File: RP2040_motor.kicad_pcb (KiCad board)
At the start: 4 copper layers, 85.5 x 54 mm, 180 parts, among them J1 USB_C_Receptacle_USB2.0, J2 Conn_01x05, J3 Conn_01x06, J4 Conn_01x04, J5 Conn_01x04, J6 Conn_01x03, SW1 SW_MEC_5G, U1 EG2131, U10 EG2131, U11 RP2040, U12 EG2131, U13 ADC081S021CISD/NOPB, U2 EG2131, U3 LM358, U4 EG2131, U5 EG2131, U6 NCP1117-3.3_SOT223, U7 XL7045, U8 LM358, U9 W25Q128JVS, Y1 Crystal_GND24

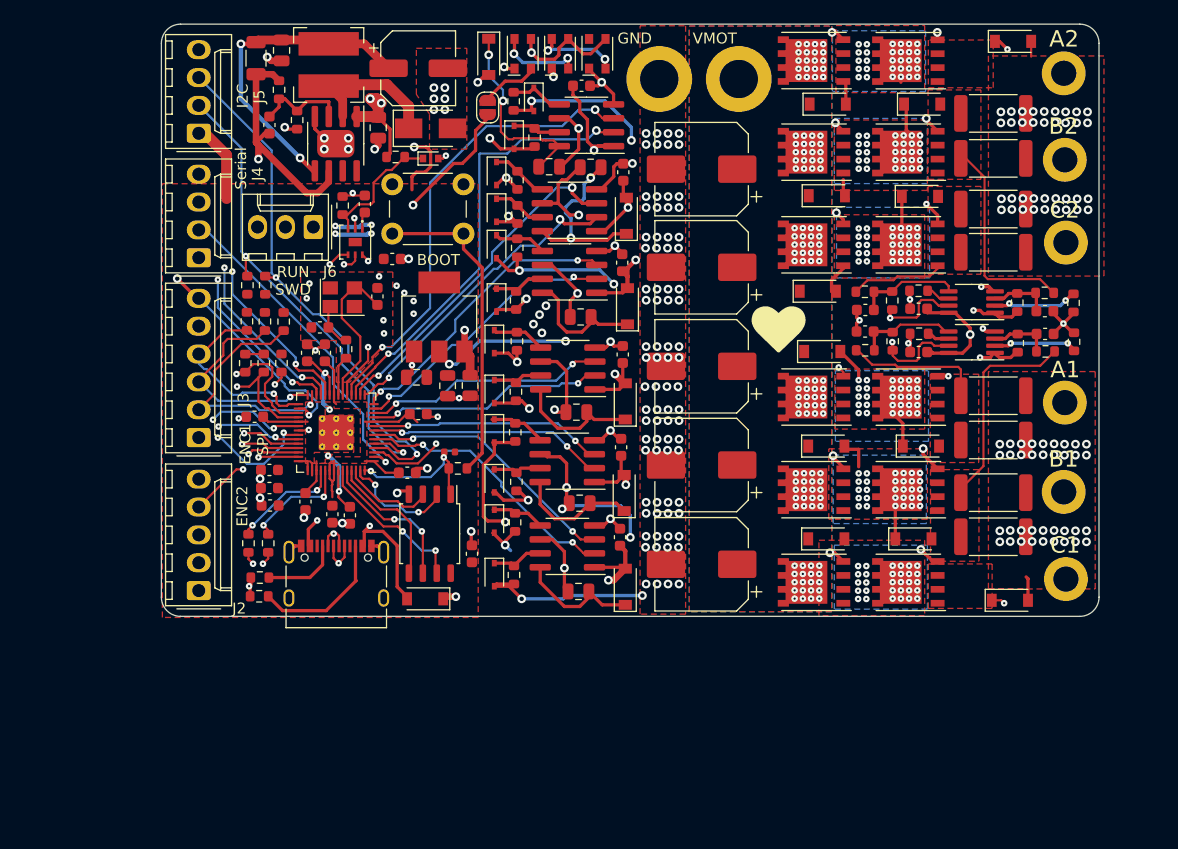
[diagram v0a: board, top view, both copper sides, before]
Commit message: Updated PCB design based on feedback. Added thermistors, mounting holes. This design has better current carrying capacity. gerber folder may not be perfect right now.
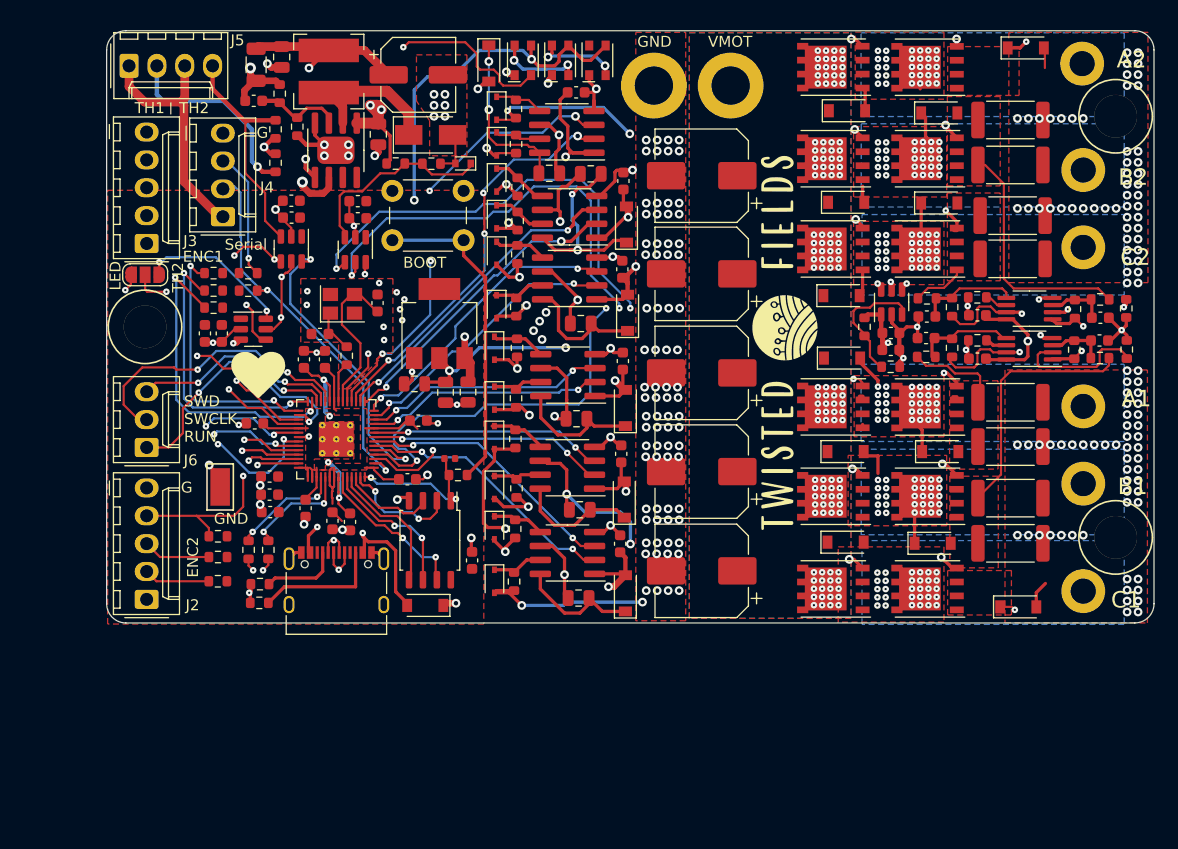
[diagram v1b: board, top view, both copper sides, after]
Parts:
- removed C13: HIGHCURRENTPAD2, RP2040_minimal:PAD_12GA_WIRE
- added C41: 1u, Capacitor_SMD:C_0603_1608Metric, F.Cu at (79.4, 95.6)
- added C42: 1u, Capacitor_SMD:C_0603_1608Metric, F.Cu at (87.3, 83.5)
- added C43: 1u, Capacitor_SMD:C_0603_1608Metric, F.Cu at (141.9, 97.1)
- added G***: LOGO, taylor_footprints:twisted_2, F.Cu at (131.6, 95.1)
- added G***: LOGO, taylor_footprints:twisted, F.Cu at (131.6, 106.7)
- added G***: LOGO, taylor_footprints:twisted_icon, F.Cu at (132.3, 94.9)
- added H1: MountingHole, RP2040_minimal:MountingHole_3.9mm_Plastite_#6, F.Cu at (162.4, 114.2)
- added H2: MountingHole, RP2040_minimal:MountingHole_3.9mm_Plastite_#6, F.Cu at (162.4, 75.8)
- added H3: MountingHole, RP2040_minimal:MountingHole_3.9mm_Plastite_#6, F.Cu at (74.0, 95.0)
- added M2C1: HIGHCURRENTPAD2, RP2040_minimal:PAD_12GA_WIRE, F.Cu at (159.5, 87.8)
- added R60: 0.1uF, Capacitor_SMD:C_0603_1608Metric, F.Cu at (81.0, 95.6)
- added R61: 10k, Resistor_SMD:R_0603_1608Metric, F.Cu at (85.8, 80.0)
- added R62: 0.1uF, Capacitor_SMD:C_0603_1608Metric, F.Cu at (87.3, 85.0)
- added R63: 10k, Resistor_SMD:R_0603_1608Metric, F.Cu at (85.8, 77.0)
- added R64: 0.1uF, Capacitor_SMD:C_0603_1608Metric, F.Cu at (142.0, 95.6)
- added R65: 10k, Resistor_SMD:R_0603_1608Metric, F.Cu at (141.9, 98.6)
- added TH1: Thermistor 10k, Resistor_SMD:R_0603_1608Metric, F.Cu at (139.6, 95.0)
- added TP2: TestPoint, TestPoint:TestPoint_Keystone_5019_Minature, F.Cu at (80.8, 109.6)
- added U14: ADC081S021CISD/NOPB, Package_TO_SOT_SMD:SOT-23-6, F.Cu at (83.8, 95.2)
- added U15: ADC081S021CISD/NOPB, Package_TO_SOT_SMD:SOT-23-6, F.Cu at (87.3, 87.9)
- added U16: ADC081S021CISD/NOPB, Package_TO_SOT_SMD:SOT-23-6, F.Cu at (142.0, 92.7)
- J3: value Conn_01x06 -> Conn_01x05; footprint Connector_Molex:Molex_KK-254_AE-6410-06A_1x06_P2.54mm_Vertical -> Connector_Molex:Molex_KK-254_AE-6410-05A_1x05_P2.54mm_Vertical
- JP1: value SolderJumper_2_Open -> SolderJumper_3_Open; footprint Jumper:SolderJumper-2_P1.3mm_Open_RoundedPad1.0x1.5mm -> Jumper:SolderJumper-3_P1.3mm_Open_RoundedPad1.0x1.5mm_NumberLabels
- R20, R22, R24, R26, R3, R4, R54, R55, R56, R57: value 22R -> 10.2R
- U13: footprint ADC081S021:ADC081S021CISD&slash_NOPB -> Package_TO_SOT_SMD:SOT-23-6
- U9: value W25Q128JVS -> W25Q16JVSSIQ
- moved JP1 34.8 mm to (74.0, 90.2), turned to 0 degrees
- moved J6 25.2 mm to (74.1, 106.0), turned to 90 degrees
- moved R45 20.0 mm to (80.6, 118.2), turned to 180 degrees
- moved J3 18.3 mm to (74.1, 87.4)
- moved R43 18.2 mm to (80.6, 116.0), turned to 180 degrees
- moved R41 16.8 mm to (80.6, 114.1), turned to 180 degrees
- moved R59 8.95 mm to (100.1, 80.1), turned to 0 degrees
- moved J5 8.85 mm to (72.5, 71.2), turned to 0 degrees
- moved R44 6.51 mm to (80.2, 93.2), turned to 180 degrees
- moved R46 6.13 mm to (93.3, 83.5), turned to 180 degrees
- moved R13 5.69 mm to (145.2, 92.4)
- moved R14 5.64 mm to (145.2, 94.1)
- moved R8 5.59 mm to (145.2, 96.0)
- moved R7 5.59 mm to (145.2, 97.7)
- moved R29 5.49 mm to (147.5, 93.2)
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- renumbered A1 to M1A1, B1 to M1B1, C12 to M1C1, A2 to M2A1, B2 to M2B1
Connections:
- net ADC_CS renamed ADC_CS1
- D34 pad 2: Net-(D34-Pad2) -> LED
- J5 pad 2: SCLK -> TH1
- J5 pad 3: SDA -> +3V3
- J5 pad 4: GND -> TH2
- JP1 pad 1: SPI0TX -> LED
- JP1 pad 2: Net-(D34-Pad2) -> LED_OR_ADC_CS4
- R49 pad 2: SDA -> TXO
- R50 pad 1: SCLK -> RXI
- U11 pad 30: SPI0TX -> LED_OR_ADC_CS4
- U11 pad 4: SDA -> ADC_CS2
- U11 pad 5: SCLK -> ADC_CS3
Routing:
- net ADC_CLK: track 30.4 -> 111.2 mm, vias 3 -> 8
- net SPI0TX: track 67.3 -> 0.00 mm, vias 3 -> 0
- net ADC_CS2: track 0.00 -> 62.4 mm, vias 0 -> 3
- net LED: track 0.00 -> 61.9 mm, vias 0 -> 2
- net ADC_DATA: track 48.4 -> 106.1 mm, vias 3 -> 7
- net SDA: track 49.1 -> 0.00 mm, vias 2 -> 0
- net SCLK: track 45.0 -> 0.00 mm, vias 2 -> 0
- net TH1: track 0.00 -> 35.8 mm, vias 0 -> 2
- net ADC_CS3: track 0.00 -> 28.4 mm, vias 0 -> 2
- net GND: track 78.6 -> 105.0 mm, vias 202 -> 229
- net LED_OR_ADC_CS4: track 0.00 -> 26.2 mm, vias 0 -> 4
- net TH2: track 0.00 -> 21.1 mm
- net +3V3: track 140.0 -> 160.6 mm, vias 9 -> 6
- net SPI0SCK: track 17.3 -> 36.5 mm, vias 1 -> 2
- net SPI0CS: track 19.6 -> 35.3 mm, vias 1 -> 2
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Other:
- board size 85.5 x 54 mm -> 95.5 x 54 mm
- board text added: "ENC1"
- board text added: "G"
- board text added: "Love everyone."
- board text added: "RUN"
- board text added: "SWCLK"
- board text added: "SWD"
- board text added: "SWD SWCLK RUN"
- board text added: "TH1 TH2"
- board text added: "TH2 | TH1"
- board text added: "|"
- board text removed: "ENC1 SPI"
- board text removed: "I2C"
- board text removed: "RUN SWD"
- board text removed: "SPI/ENC1"

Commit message: Additional updates to clean up power and capacitance on buck circuit.
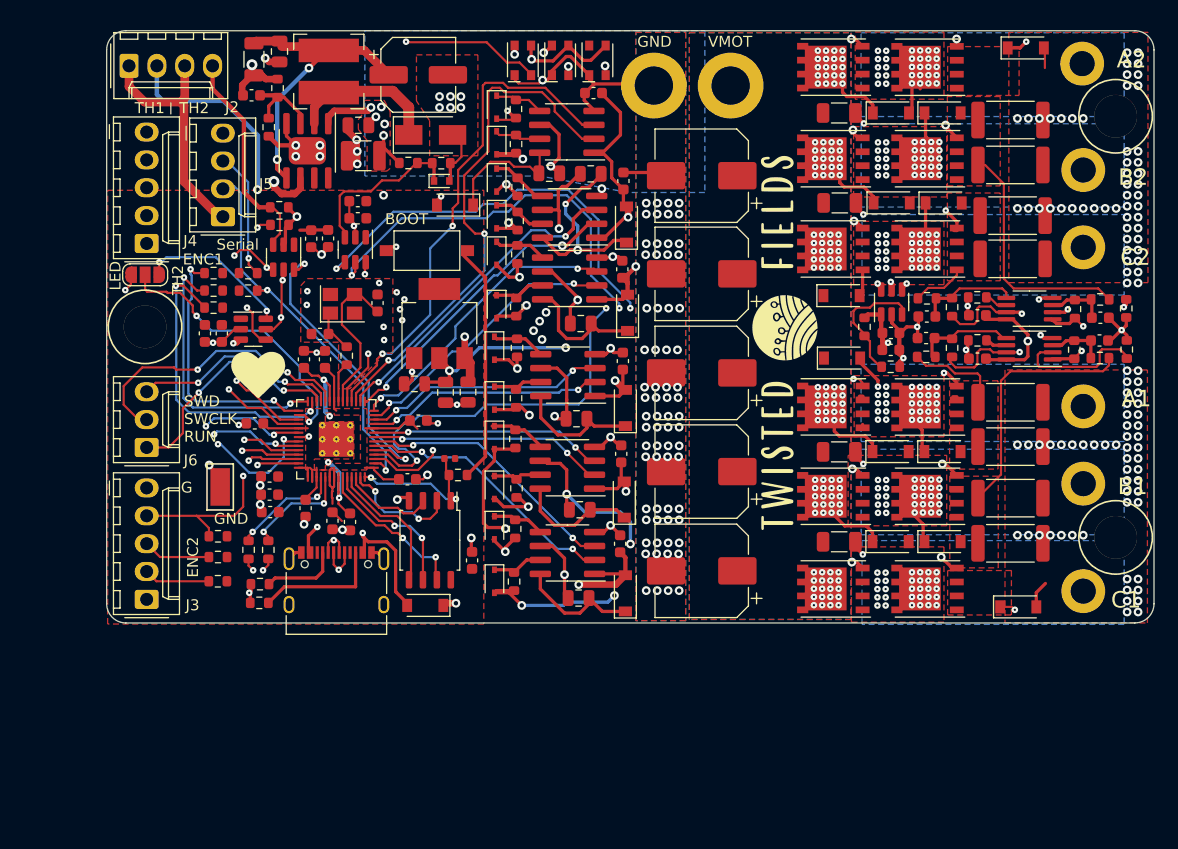
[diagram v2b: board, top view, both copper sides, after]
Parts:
- added C$1: 2.2uF 100V, Capacitor_SMD:C_1206_3216Metric, F.Cu at (137.2, 75.5)
- added C$2: 2.2uF 100V, Capacitor_SMD:C_1206_3216Metric, F.Cu at (137.2, 106.4)
- added C$3: 2.2uF 100V, Capacitor_SMD:C_1206_3216Metric, F.Cu at (137.3, 83.7)
- added C$4: 2.2uF 100V, Capacitor_SMD:C_1206_3216Metric, F.Cu at (137.2, 114.6)
- added C$5: 4.7uF 100V, Capacitor_SMD:C_1210_3225Metric, F.Cu at (93.8, 79.4)
- SW1: footprint Button_Switch_THT:SW_PUSH_6mm_H4.3mm -> parts:SW_TS_1101_C_W
- moved D24 13.3 mm to (102.2, 83.9), turned to 180 degrees
- moved R51 7.12 mm to (86.2, 84.1), turned to 0 degrees
- moved SW1 6.29 mm to (99.7, 88.0)
- moved R46 5.67 mm to (86.2, 85.7), turned to 0 degrees
- moved D19 4.15 mm to (142.0, 83.7)
- moved D7 4.10 mm to (141.9, 114.6)
- moved D17 4.10 mm to (141.9, 106.4)
- moved D29 4.00 mm to (142.0, 75.5)
- moved C22 3.90 mm to (89.1, 87.0), turned to 90 degrees
- moved R47 3.83 mm to (90.6, 86.9), turned to -90 degrees
- moved R49 2.60 mm to (85.2, 76.8)
- moved U11 2.60 mm to (88.8, 79.0)
- moved D36 2.52 mm to (101.0, 81.7), turned to 0 degrees
- moved C$6 1.99 mm to (93.4, 76.6), turned to 180 degrees
- moved C15 1.58 mm to (114.8, 73.7), turned to 0 degrees
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- renumbered C$1 to C$6, C$2 to C$7, C2 to C1, C14 to C10, C15 to C11, C17 to C12, C18 to C13, C21 to C14, C24 to C15, C26 to C16, C28 to C17, C43 to C18, C41 to C19, C3 to C2, C16 to C20, C20 to C21, C42 to C22, C19 to C23, C22 to C24, C27 to C26, C9 to C27, C10 to C28, C23 to C29, C6 to C3, C29 to C30, C30 to C31, C31 to C32, C32 to C33, C33 to C34, C34 to C35, C35 to C36, C36 to C37, C37 to C38, C38 to C39, C11 to C4, C39 to C40, C40 to C41, C1 to C5, C4 to C6, C5 to C7, C7 to C8, C8 to C9, D13 to D12, D14 to D13, D12 to D14, D20 to D19, D21 to D20, D23 to D21, D25 to D22, D26 to D23, D27 to D25, D28 to D26, D29 to D27, D30 to D28, D31 to D29, D32 to D30, D19 to D31, D22 to D32, D34 to D33, D35 to D34, D36 to D35, D33 to D36, J5 to J2, J2 to J3, J3 to J4, J4 to J5, R34 to R1, R29 to R10, R5 to R11, R6 to R12, R28 to R13, R11 to R14, R30 to R15, R12 to R16, R31 to R17, R37 to R18, R20 to R19, R36 to R2, R22 to R20, R38 to R21, R33 to R22, R52 to R23, R26 to R25, R53 to R26, R39 to R27, R58 to R28, R15 to R29, R13 to R3, R19 to R30, R7 to R31, R8 to R32, R9 to R33, R54 to R34, R55 to R35, R10 to R36, R56 to R37, R57 to R38, R64 to R39, R1 to R4, R60 to R40, R23 to R41, R25 to R42, R16 to R43, R17 to R44, R65 to R45, R61 to R46, R62 to R47, R27 to R48, R32 to R49, R2 to R5, R35 to R50, R63 to R51, R21 to R52, R40 to R53, R41 to R54, R42 to R55, R43 to R56, R44 to R57, R45 to R58, R46 to R59, R14 to R6, R47 to R60, R48 to R61, R49 to R62, R50 to R63, R51 to R64, R59 to R65, R3 to R7, R4 to R8, R18 to R9, U14 to U10, U7 to U11, U9 to U12, U6 to U13, U15 to U14, U11 to U15, U13 to U16, U8 to U3, U3 to U6, U10 to U7, U12 to U8, U16 to U9
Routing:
- net GND: track 105.0 -> 131.4 mm, vias 229 -> 226
- net VMOT: track 47.9 -> 29.6 mm, vias 122 -> 125
- net GPIO14: track 36.7 -> 48.5 mm, vias 4 -> 2
- net /power_and_cpu/~{USB_BOOT}: track 29.4 -> 21.5 mm
- net Net-(AH2-Pad2): track 44.3 -> 51.8 mm
- net +12V: track 215.3 -> 209.0 mm, vias 11 -> 10
- net GPIO15: track 40.9 -> 46.1 mm, vias 4 -> 2
- net Net-(C17-Pad2): track 15.9 -> 11.4 mm, vias 2 -> 0
- net ADC_DATA: track 106.1 -> 102.6 mm
- net Net-(D36-Pad1): track 18.4 -> 15.1 mm
- net +3V3: track 160.6 -> 163.8 mm
- net M1B: track 48.3 -> 45.1 mm
- net ADC_CLK: track 111.2 -> 108.4 mm
- net Net-(BL1-Pad2): track 59.9 -> 57.8 mm
- net LED: track 61.9 -> 59.9 mm
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- added copper zone on B.Cu, net GND

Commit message: updated design with dual CPUs
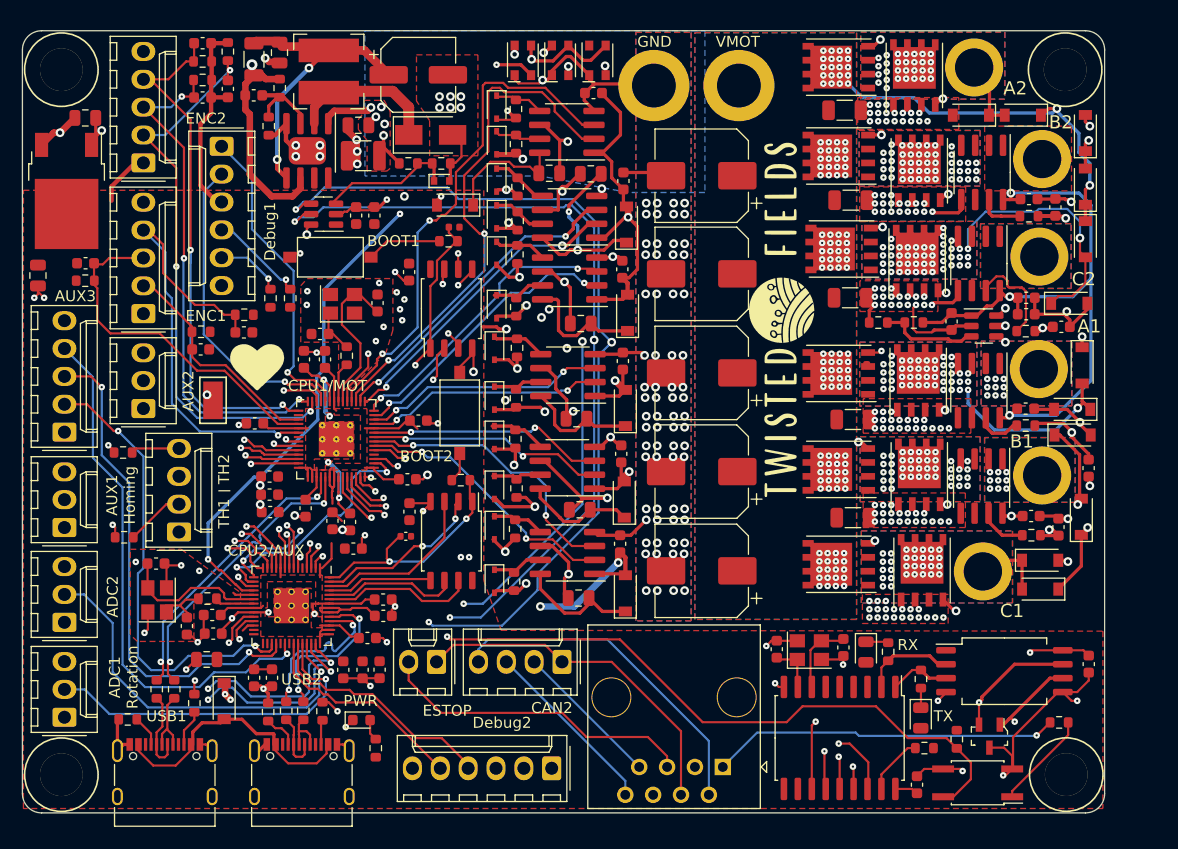
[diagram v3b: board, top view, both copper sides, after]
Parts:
- removed D31: B5819W SL, Diode_SMD:D_SOD-123
- removed JP1: SolderJumper_3_Open, Jumper:SolderJumper-3_P1.3mm_Open_RoundedPad1.0x1.5mm_NumberLabels
- removed R10, R22, R26, R36: 133k, Resistor_SMD:R_0603_1608Metric
- removed R11, R12, R14, R16, R29, R30: 4mΩ, Resistor_SMD:R_2512_6332Metric
- removed R13, R18, R31: 499R, Resistor_SMD:R_0603_1608Metric
- removed R15, R21, R27, R28, R32: 0.1uF, Capacitor_SMD:C_0603_1608Metric
- removed R17, R23, R33, R9: 4.64k, Resistor_SMD:R_0603_1608Metric
- removed U6: LM358, Package_SO:MSOP-8_3x3mm_P0.65mm
- added C$8: 2.2uF 100V, Capacitor_SMD:C_1206_3216Metric, F.Cu at (138.5, 103.5)
- added C42: 20p, Capacitor_SMD:C_0603_1608Metric, F.Cu at (77.8, 122.3)
- added C43: 100n, Capacitor_SMD:C_0603_1608Metric, F.Cu at (98.1, 111.9)
- added C44: 100n, Capacitor_SMD:C_0603_1608Metric, F.Cu at (94.2, 123.4)
- added C45: 100n, Capacitor_SMD:C_0603_1608Metric, F.Cu at (80.2, 123.0)
- added C46: 100n, Capacitor_SMD:C_0603_1608Metric, F.Cu at (95.7, 121.4)
- added C47: 100n, Capacitor_SMD:C_0603_1608Metric, F.Cu at (83.9, 127.0)
- added C48: 100n, Capacitor_SMD:C_0603_1608Metric, F.Cu at (85.5, 127.0)
- added C49: 100n, Capacitor_SMD:C_0603_1608Metric, F.Cu at (92.9, 115.2)
- added C50: 100n, Capacitor_SMD:C_0603_1608Metric, F.Cu at (80.1, 121.3)
- added C51: 100n, Capacitor_SMD:C_0603_1608Metric, F.Cu at (92.0, 126.3)
- added C52: 100n, Capacitor_SMD:C_0603_1608Metric, F.Cu at (93.8, 126.3)
- added C53: 1u, Capacitor_SMD:C_0603_1608Metric, F.Cu at (95.7, 119.9)
- added C54: 1u, Capacitor_SMD:C_0603_1608Metric, F.Cu at (95.3, 126.3)
- added C55: 0.1uF, Capacitor_SMD:C_0603_1608Metric, F.Cu at (160.0, 125.8)
- added C56: 100n, Capacitor_SMD:C_0603_1608Metric, F.Cu at (144.3, 136.8)
- added C57: 10p, Capacitor_SMD:C_0603_1608Metric, F.Cu at (137.6, 124.2)
- added C58: 10p, Capacitor_SMD:C_0603_1608Metric, F.Cu at (131.6, 124.4)
- added C59: 0.1uF, Capacitor_SMD:C_0603_1608Metric, F.Cu at (154.3, 92.3)
- added C60: 47p, Capacitor_SMD:C_0603_1608Metric, F.Cu at (83.0, 95.5)
- added C61: 47p, Capacitor_SMD:C_0603_1608Metric, F.Cu at (68.5, 89.2)
- added C62: 47p, Capacitor_SMD:C_0603_1608Metric, F.Cu at (79.0, 97.1)
- added C63: 47p, Capacitor_SMD:C_0603_1608Metric, F.Cu at (79.2, 74.1)
- added C64: 47p, Capacitor_SMD:C_0603_1608Metric, F.Cu at (81.5, 73.3)
- added C65: 0.1uF, Capacitor_SMD:C_0603_1608Metric, F.Cu at (157.5, 95.0)
- added C66: 0.1uF, Capacitor_SMD:C_0603_1608Metric, F.Cu at (154.6, 83.3)
- added C67: 0.1uF, Capacitor_SMD:C_0603_1608Metric, F.Cu at (154.8, 112.2)
- added C68: 0.1uF, Capacitor_SMD:C_0603_1608Metric, F.Cu at (154.2, 102.5)
- added C69: 0.1uF, Capacitor_SMD:C_0603_1608Metric, F.Cu at (157.2, 113.3)
- added C70: 0.1uF, Capacitor_SMD:C_0603_1608Metric, F.Cu at (157.0, 84.1)
- added C71: 0.1uF, Capacitor_SMD:C_0603_1608Metric, F.Cu at (160.0, 107.9)
- added D37: B5819W SL, Diode_SMD:D_SOD-123, F.Cu at (81.2, 129.1)
- added D38: LED_GREEN, LED_SMD:LED_0805_2012Metric, F.Cu at (144.7, 130.7)
- added D39: LED_ORANGE_RED, LED_SMD:LED_0805_2012Metric, F.Cu at (139.7, 124.7)
- added D40: CDSOT23-SM712, digikey-footprints:SOT-23-3, F.Cu at (150.9, 132.3)
- added D41: LED_RED, LED_SMD:LED_0603_1608Metric, F.Cu at (93.7, 130.9)
- added H4: MountingHole, RP2040_minimal:MountingHole_3.9mm_Plastite_#6, F.Cu at (66.3, 71.5)
- added J10: Conn_01x03, Connector_Molex:Molex_KK-254_AE-6410-03A_1x03_P2.54mm_Vertical, F.Cu at (66.6, 113.3)
- added J11: Conn_01x04, Connector_Molex:Molex_KK-254_AE-6410-04A_1x04_P2.54mm_Vertical, F.Cu at (112.0, 125.5)
- added J12: Conn_01x06, Connector_Molex:Molex_KK-254_AE-6410-06A_1x06_P2.54mm_Vertical, F.Cu at (111.0, 135.3)
- added J13: Conn_01x03, Connector_Molex:Molex_KK-254_AE-6410-03A_1x03_P2.54mm_Vertical, F.Cu at (66.6, 121.9)
- added J14: Conn_01x03, Connector_Molex:Molex_KK-254_AE-6410-03A_1x03_P2.54mm_Vertical, F.Cu at (73.8, 102.5)
- added J15: Conn_01x05, Connector_Molex:Molex_KK-254_AE-6410-05A_1x05_P2.54mm_Vertical, F.Cu at (66.6, 104.6)
- added J7: Conn_01x02, Connector_Molex:Molex_KK-254_AE-6410-02A_1x02_P2.54mm_Vertical, F.Cu at (100.5, 125.5)
- added J8: RJ45, Connector_RJ:RJ45_OST_PJ012-8P8CX_Vertical, F.Cu at (126.6, 135.1)
- added J9: Conn_01x03, Connector_Molex:Molex_KK-254_AE-6410-03A_1x03_P2.54mm_Vertical, F.Cu at (66.6, 130.6)
- added R46: 5.1k, Resistor_SMD:R_0603_1608Metric, F.Cu at (90.1, 130.0)
- added R51: DNS, Capacitor_SMD:C_0402_1005Metric, F.Cu at (97.7, 114.1)
- added R66: 1.1k, Resistor_SMD:R_0603_1608Metric, F.Cu at (102.7, 109.0)
- added R67: 1k, Resistor_SMD:R_0603_1608Metric, F.Cu at (144.7, 127.1)
- added R68: 1k, Resistor_SMD:R_0603_1608Metric, F.Cu at (141.7, 124.6)
- added R70: 27, Resistor_SMD:R_0603_1608Metric, F.Cu at (88.4, 130.0)
- added R71: 27, Resistor_SMD:R_0603_1608Metric, F.Cu at (86.8, 130.0)
- added R72: 10k, Resistor_SMD:R_0603_1608Metric, F.Cu at (145.0, 133.4)
- added R75: 100R, Resistor_SMD:R_0603_1608Metric, F.Cu at (157.3, 131.1)
- added R76: 5.1k, Resistor_SMD:R_0603_1608Metric, F.Cu at (148.0, 132.6)
- added R77: 68R, Resistor_SMD:R_0603_1608Metric, F.Cu at (95.0, 133.4)
- added SW2: SW_MEC_5G, parts:SW_TS_1101_C_W, F.Cu at (102.6, 102.8)
- added U17: isolator, Package_SO:SOIC-8_7.5x5.85mm_P1.27mm, F.Cu at (152.3, 126.4)
- added U18: MCP2515-xSO, Package_SO:SOIC-18W_7.5x11.6mm_P1.27mm, F.Cu at (137.3, 132.5)
- added U19: RP2040, RP2040_minimal:RP2040-QFN-56, F.Cu at (87.3, 120.4)
- added U20: CC6920B, Package_SO:SOIC-8_3.9x4.9mm_P1.27mm, F.Cu at (150.2, 109.5)
- added U21: EL357N(C)(TA)-G, Package_SO:SO-4_4.4x3.6mm_P2.54mm, F.Cu at (149.9, 136.6)
- added U22: CC6920B, Package_SO:SOIC-8_3.9x4.9mm_P1.27mm, F.Cu at (150.0, 100.8)
- added Y2: Crystal_GND24, Crystal:Crystal_SMD_3225-4Pin_3.2x2.5mm, F.Cu at (75.1, 119.9)
- added Y3: Crystal_GND24, Crystal:Crystal_SMD_3225-4Pin_3.2x2.5mm, F.Cu at (134.5, 124.5)
- C19: value 1u -> 20p
- C22: value 1u -> 10u; footprint Capacitor_SMD:C_0603_1608Metric -> Capacitor_SMD:C_0805_2012Metric
- C23: value 10u -> 47p; footprint Capacitor_SMD:C_0805_2012Metric -> Capacitor_SMD:C_0603_1608Metric
- J5: value Conn_01x04 -> Conn_01x06; footprint Connector_Molex:Molex_KK-254_AE-6410-04A_1x04_P2.54mm_Vertical -> Connector_Molex:Molex_KK-254_AE-6410-06A_1x06_P2.54mm_Vertical
- J6: value Conn_01x03 -> USB_C_Receptacle_USB2.0; footprint Connector_Molex:Molex_KK-254_AE-6410-03A_1x03_P2.54mm_Vertical -> Connector_USB:USB_C_Receptacle_XKB_U262-16XN-4BVC11
- R1, R2: value 4mΩ -> 330R; footprint Resistor_SMD:R_2512_6332Metric -> Resistor_SMD:R_0603_1608Metric
- R3: value 499R -> 330R
- R40: value 0.1uF -> 5.1k; footprint Capacitor_SMD:C_0603_1608Metric -> Resistor_SMD:R_0603_1608Metric
- R47: value 0.1uF -> 1.1k; footprint Capacitor_SMD:C_0603_1608Metric -> Resistor_SMD:R_0603_1608Metric
- R53, R54, R55, R56, R57, R58: value 23.2k -> 10k
- R6: value 0.1uF -> 330R; footprint Capacitor_SMD:C_0603_1608Metric -> Resistor_SMD:R_0603_1608Metric
- U10: value ADC081S021CISD/NOPB -> LD1086DT33TR; footprint Package_TO_SOT_SMD:SOT-23-6 -> Package_TO_SOT_SMD:TO-252-2
- U13: value NCP1117-3.3_SOT223 -> W25Q16JVSSIQ; footprint Package_TO_SOT_SMD:SOT-223-3_TabPin2 -> Package_SO:SOIC-8_5.23x5.23mm_P1.27mm
- U14: value ADC081S021CISD/NOPB -> CC6920B; footprint Package_TO_SOT_SMD:SOT-23-6 -> Package_SO:SOIC-8_3.9x4.9mm_P1.27mm
- U3: value LM358 -> CC6920B; footprint Package_SO:MSOP-8_3x3mm_P0.65mm -> Package_SO:SOIC-8_3.9x4.9mm_P1.27mm
- moved U14 64.2 mm to (150.3, 80.9)
- moved C20 42.9 mm to (68.5, 76.0), turned to 0 degrees
- moved J2 42.8 mm to (77.0, 113.7), turned to 90 degrees
- moved H3 41.5 mm to (66.3, 135.8)
- moved C23 36.6 mm to (79.2, 69.1)
- moved R40 34.8 mm to (85.2, 130.1)
- moved R47 34.6 mm to (79.6, 119.8), turned to 180 degrees
- moved J6 33.8 mm to (88.2, 136.8), turned to 0 degrees
- moved C29 32.7 mm to (79.6, 125.3), turned to 180 degrees
- moved R74 31.8 mm to (72.0, 114.2), turned to 180 degrees
- moved R2 29.2 mm to (154.8, 114.0), turned to 0 degrees
- moved R56 28.0 mm to (68.5, 90.8), turned to 0 degrees
- moved C21 26.9 mm to (98.0, 90.0), turned to -90 degrees
- moved R79 26.5 mm to (72.0, 106.5), turned to 180 degrees
- moved J3 26.1 mm to (73.8, 93.8)
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- renumbered R46 to R74, R51 to R79
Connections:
- net ENCA renamed ENC1_RX
- net ENCB renamed ENC1_CS
- net SPI0CS renamed ENC2_CS
- net SPI0RX renamed ENC2_RX
- AL1 pad 1: VSENSE1A -> GND
- BL1 pad 1: VSENSE1B -> GND
- BL2 pad 1: VSENSE2B -> GND
- C19 pad 1: GND -> /power_and_cpu/XIN_2
- C19 pad 2: +3V3 -> GND
- C22 pad 1: GND -> +3V3
- C22 pad 2: +3V3 -> GND
- C23 pad 2: GND -> ENC2_SCK
- C9 pad 1: M2C -> Net-(C9-Pad1)
- CH2 pad 1: M2C -> Net-(C9-Pad1)
- CL2 pad 1: VSENSE2C -> GND
- CL2 pad 3: M2C -> Net-(C9-Pad1)
- D10 pad 1: M2C -> Net-(C9-Pad1)
- D10 pad 2: VSENSE2C -> GND
- D18 pad 2: VSENSE1B -> GND
- D20 pad 2: VSENSE2B -> GND
- D28 pad 2: VSENSE1A -> GND
- D9 pad 2: M2C -> Net-(C9-Pad1)
- J2 pad 2: TH1 -> A3_2
- J2 pad 4: TH2 -> A4_2
- J3 pad 4: ENCC -> ENC1_SCK
- J4 pad 4: SPI0SCK -> ENC2_SCK
- J5 pad 1: +3V3 -> SWCLK
- J5 pad 2: TXO -> SWD
- J5 pad 3: RXI -> +3V3
- J5 pad 4: GND -> RXI
- M1A1 pad 1: M1A -> M1A1
- M1B1 pad 1: M1B -> M1B1
- M2B1 pad 1: M2B -> M2B1
- M2C1 pad 1: M2C -> M2C1
- R1 pad 1: GND -> Net-(R1-Pad1)
- R1 pad 2: VSENSE2C -> A2
- R2 pad 1: GND -> Net-(R2-Pad1)
- R2 pad 2: VSENSE2C -> A4
- R3 pad 1: VSENSE2C -> Net-(R3-Pad1)
- R3 pad 2: Net-(R10-Pad2) -> A1
- R40 pad 1: +3V3 -> GND
- R40 pad 2: GND -> Net-(J6-PadA5)
- R47 pad 1: +3V3 -> /power_and_cpu/XOUT_2
- R47 pad 2: GND -> Net-(C42-Pad1)
- R53 pad 2: SPI0SCK -> ENC2_SCK
- R54 pad 2: ENCC -> ENC1_SCK
- R6 pad 1: Net-(R10-Pad2) -> Net-(R6-Pad1)
- R6 pad 2: GND -> A3
- R74 pad 1: TH1 -> A3_2
- R79 pad 1: TH2 -> A4_2
- U10 pad 1: +3V3 -> GND
- U10 pad 2: GND -> +3V3
- U10 pad 3: TH1 -> +12V
- U13 pad 1: GND -> /power_and_cpu/QSPI_SS_2
- U13 pad 2: +3V3 -> /power_and_cpu/QSPI_SD1_2
- U13 pad 3: +12V -> /power_and_cpu/QSPI_SD2_2
- U14 pad 1: +3V3 -> M2B1
- U14 pad 2: GND -> M2B1
- U14 pad 3: TH2 -> M2B
- U14 pad 4: ADC_CLK -> M2B
- U14 pad 5: ADC_DATA -> GND
- U14 pad 6: ADC_CS3 -> unconnected-(U14-Pad6)
- U15 pad 2: TXO -> TXO_RX2
- U15 pad 24: /power_and_cpu/SWCLK -> SWCLK
- U15 pad 25: /power_and_cpu/SWD -> SWD
- U15 pad 26: /power_and_cpu/RUN -> +3V3
- U15 pad 29: SPI0SCK -> ENC2_SCK
- U15 pad 3: RXI -> RXI_TX2
- U15 pad 30: LED_OR_ADC_CS4 -> unconnected-(U15-Pad30)
- U15 pad 34: ADC_CLK -> ENC1_SCK
- U15 pad 35: ENCC -> unconnected-(U15-Pad35)
- U15 pad 36: ADC_DATA -> TXO
- U15 pad 37: ADC_CS1 -> RXI
- U15 pad 4: ADC_CS2 -> unconnected-(U15-Pad4)
- U15 pad 5: ADC_CS3 -> unconnected-(U15-Pad5)
- U2 pad 6: M2C -> Net-(C9-Pad1)
- U3 pad 1: A1 -> M2C1
- U3 pad 2: Net-(R23-Pad1) -> M2C1
- U3 pad 3: Net-(R18-Pad2) -> Net-(C9-Pad1)
- U3 pad 4: GND -> Net-(C9-Pad1)
- U3 pad 5: Net-(R10-Pad2) -> GND
- U3 pad 6: Net-(R9-Pad1) -> unconnected-(U3-Pad6)
- U3 pad 7: A2 -> Net-(R1-Pad1)
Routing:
- net ESTOP: track 0.00 -> 82.4 mm, vias 0 -> 2
- net SPI1_RX_2: track 0.00 -> 82.4 mm, vias 0 -> 2
- net SPI1_CSn_2: track 0.00 -> 80.6 mm, vias 0 -> 2
- net SPI1_SCK_2: track 0.00 -> 78.7 mm, vias 0 -> 2
- net GND_REMOTE: track 0.00 -> 77.8 mm, vias 0 -> 2
- net 5V_REMOTE: track 0.00 -> 77.5 mm, vias 0 -> 1
- net SPI1_TX_2: track 0.00 -> 76.7 mm, vias 0 -> 2
- net +3V3: track 163.8 -> 236.6 mm, vias 6 -> 8
- net SPI1_INT: track 0.00 -> 60.6 mm, vias 0 -> 2
- net GND: track 131.4 -> 191.6 mm, vias 226 -> 251
- net Net-(C9-Pad1): track 0.00 -> 60.1 mm, vias 0 -> 47
- net A4_2: track 0.00 -> 58.9 mm, vias 0 -> 2
- net VMOT: track 29.6 -> 83.0 mm, vias 125 -> 129
- net ENC2_SCK: track 0.00 -> 49.6 mm, vias 0 -> 2
- net AUX3_SCK: track 0.00 -> 49.2 mm, vias 0 -> 1
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- added copper zone on B.Cu, net M1A1
- added copper zone on F.Cu, net M1A1
- added copper zone on B.Cu, net M1B1
- added copper zone on F.Cu, net M1B1
- added copper zone on F.Cu, net M2B1
- added copper zone on B.Cu, net M2C1
- added copper zone on F.Cu, net M2C1
- added copper zone on B.Cu, net Net-(C9-Pad1)
- added copper zone on F.Cu, net Net-(C9-Pad1)
- removed copper zone on In2.Cu, net M1A
- removed copper zone on In2.Cu, net M1B
- removed copper zone on In2.Cu, net M1C
- removed copper zone on In2.Cu, net M2A
- removed copper zone on In2.Cu, net M2B
- removed copper zone on B.Cu, net M2C
- removed copper zone on F.Cu, net M2C
- removed copper zone on In2.Cu, net M2C
- removed copper zone on F.Cu, net VSENSE1A
- removed copper zone on F.Cu, net VSENSE1B
- removed copper zone on F.Cu, net VSENSE2B
- removed copper zone on F.Cu, net VSENSE2C
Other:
- board size 95.5 x 54 mm -> 98.7 x 71.3 mm
- board text added: "ADC1 Rotation"
- board text added: "ADC2"
- board text added: "AUX1 Homing"
- board text added: "AUX2"
- board text added: "AUX3"
- board text added: "BOOT1"
- board text added: "BOOT2"
- board text added: "CAN2"
- board text added: "CPU1/MOT"
- board text added: "CPU2/AUX"
- board text added: "Debug1"
- board text added: "Debug2"
- board text added: "Dual CPU Version 1"
- board text added: "ESTOP"
- board text added: "PWR"
- board text added: "RX"
- board text added: "TX"
- board text added: "USB1"
- board text added: "USB2"
- board text removed: "BOOT"
- board text removed: "G"
- board text removed: "RUN"
- board text removed: "SWCLK"
- board text removed: "SWD"
- board text removed: "SWD SWCLK RUN"
- board text removed: "Serial"
- board text removed: "Version 1"
